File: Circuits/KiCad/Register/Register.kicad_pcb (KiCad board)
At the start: 2 copper layers, 55.2 x 52.1 mm, 7 parts, among them J1 Conn_01x13_Male, J2 Conn_01x02_Male, J3 Conn_01x02_Male, U1 74LS377f, U2 74LS245

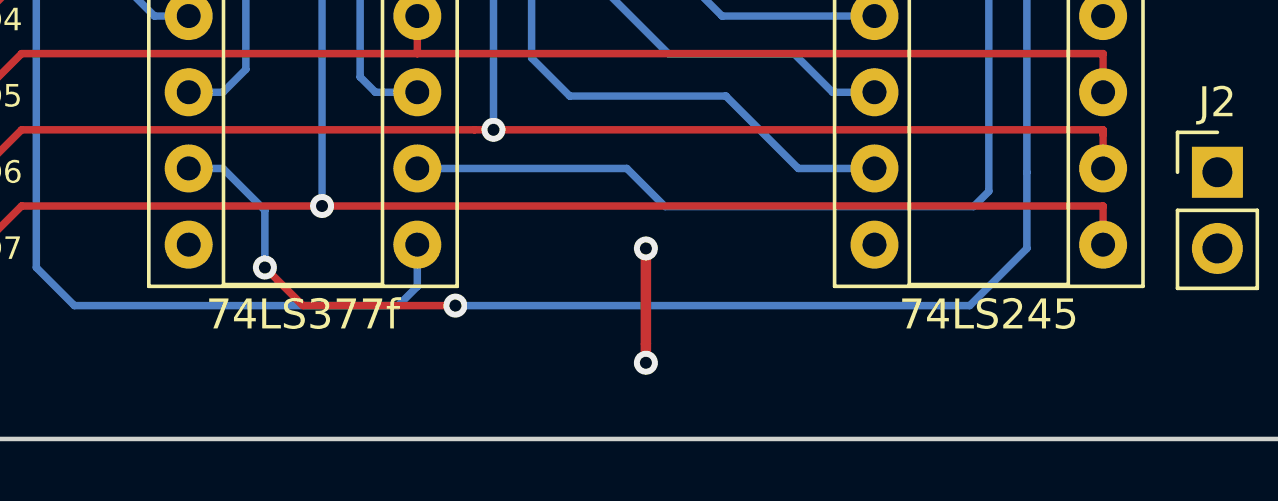
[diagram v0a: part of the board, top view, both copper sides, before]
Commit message: Added Stack Pointer schematics & PCB. Rerouted Clock based autorouter output
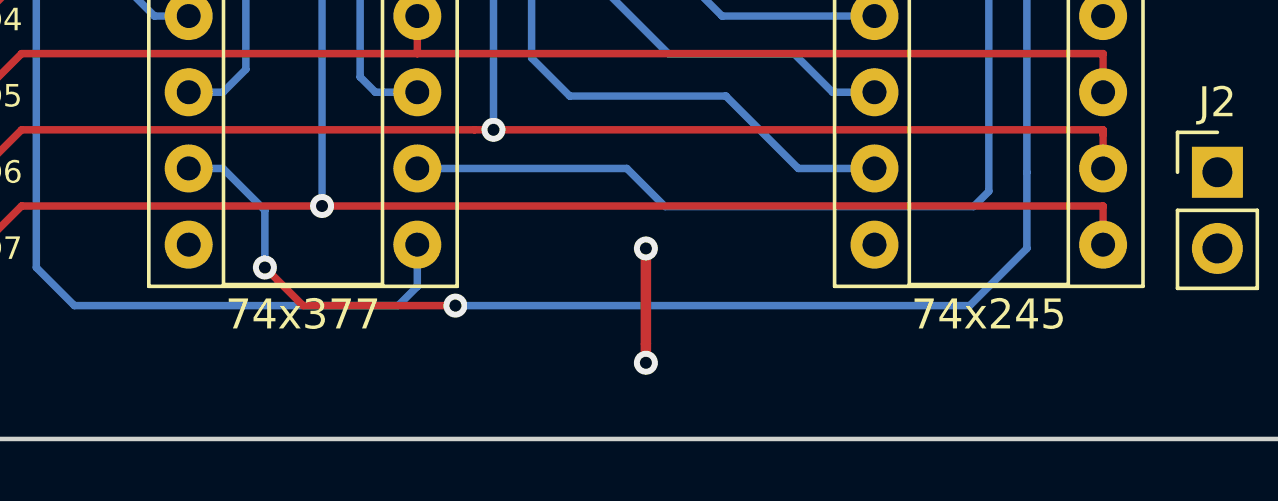
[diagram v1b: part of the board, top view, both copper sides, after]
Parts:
- U1: value 74LS377f -> 74x377
- U2: value 74LS245 -> 74x245
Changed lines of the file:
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@@
       (effects (font (size 1 1) (thickness 0.15)))
     )
-    (fp_text value 74LS245 (at 3.81 25.19) (layer F.SilkS)
+    (fp_text value 74x245 (at 3.81 25.19) (layer F.SilkS)
       (effects (font (size 1 1) (thickness 0.15)))
     )
@@
       (effects (font (size 1 1) (thickness 0.15)))
     )
-    (fp_text value 74LS377f (at 3.81 25.19) (layer F.SilkS)
+    (fp_text value 74x377 (at 3.81 25.19) (layer F.SilkS)
       (effects (font (size 1 1) (thickness 0.15)))
     )

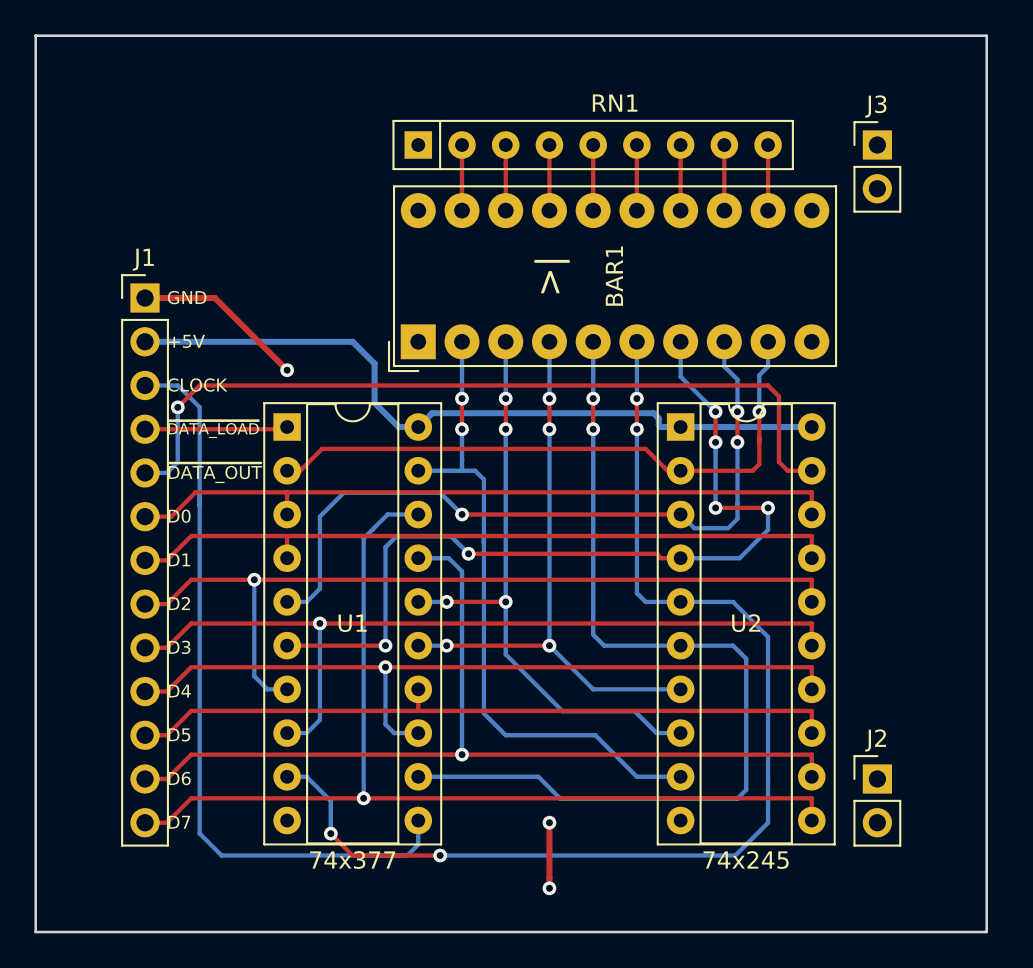
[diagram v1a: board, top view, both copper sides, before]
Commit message: Made sure spacing between headers is always 2.54mm pitch
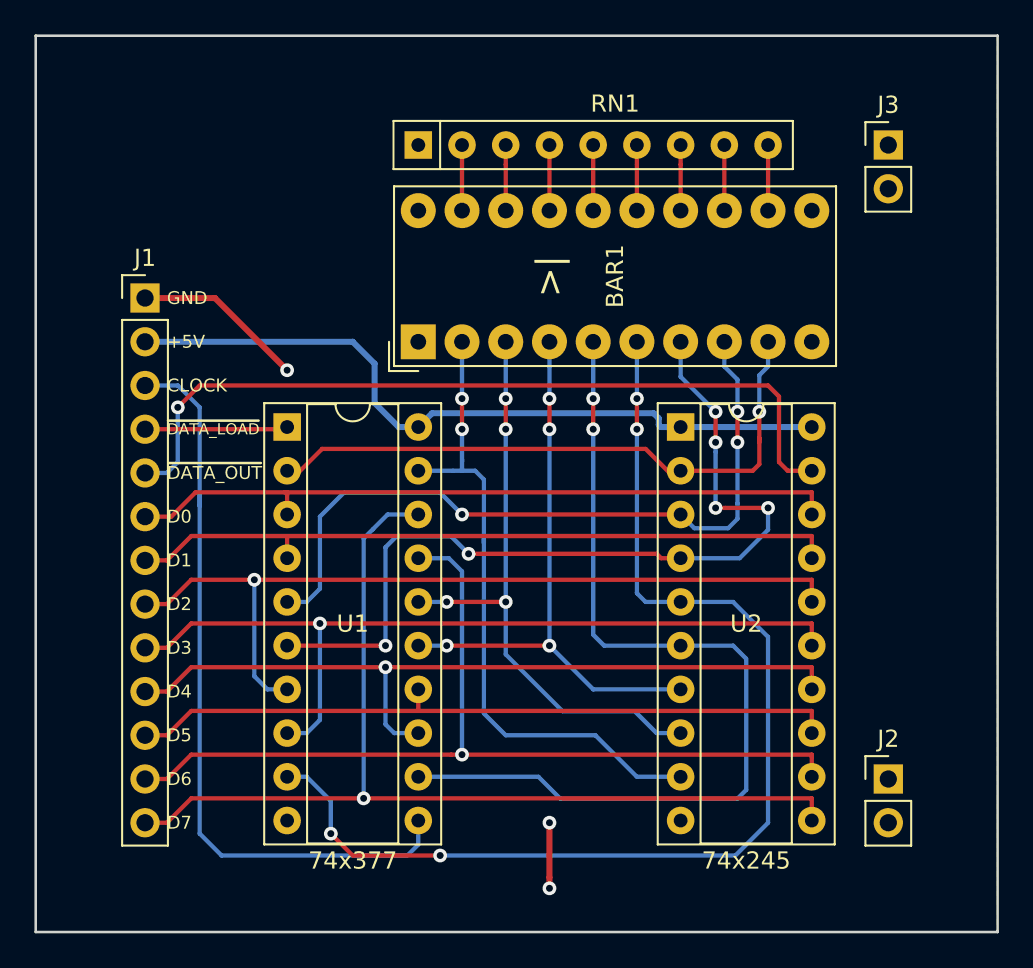
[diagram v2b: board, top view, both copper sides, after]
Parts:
- moved J2 0.63 mm to (76.8, 61.0)
- moved J3 0.63 mm to (76.8, 24.1)
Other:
- board size 55.2 x 52.1 mm -> 55.9 x 52.1 mm
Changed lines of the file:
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@@
   )
   (module Connector_PinHeader_2.54mm:PinHeader_1x02_P2.54mm_Vertical (layer F.Cu)
-    (at 76.2 24.13)
+    (at 76.835 24.13)
     (descr "Through hole straight pin header, 1x02, 2.54mm pitch, single row")
     (tags "Through hole pin header THT 1x02 2.54mm single row")
@@
   )
   (module Connector_PinHeader_2.54mm:PinHeader_1x02_P2.54mm_Vertical (layer F.Cu)
-    (at 76.2 60.96)
+    (at 76.835 60.96)
     (descr "Through hole straight pin header, 1x02, 2.54mm pitch, single row")
     (tags "Through hole pin header THT 1x02 2.54mm single row")
@@
   )
   (gr_line (start 27.305 69.85) (end 27.305 17.78) (layer Edge.Cuts) (width 0.15))
-  (gr_line (start 82.55 69.85) (end 27.305 69.85) (layer Edge.Cuts) (width 0.15))
-  (gr_line (start 82.55 17.78) (end 82.55 69.85) (layer Edge.Cuts) (width 0.15))
-  (gr_line (start 27.305 17.78) (end 82.55 17.78) (layer Edge.Cuts) (width 0.15))
+  (gr_line (start 83.185 69.85) (end 27.305 69.85) (layer Edge.Cuts) (width 0.15))
+  (gr_line (start 83.185 17.78) (end 83.185 69.85) (layer Edge.Cuts) (width 0.15))
+  (gr_line (start 27.305 17.78) (end 83.185 17.78) (layer Edge.Cuts) (width 0.15))
   (gr_text >| (at 57.15 31.75 90) (layer F.SilkS)
     (effects (font (size 1.5 1.5) (thickness 0.3)))
   )
-  (gr_poly (pts (xy 77.47 64.77) (xy 82.47 64.77) (xy 82.47 69.77) (xy 77.47 69.77)) (layer Margin) (width 0.15))
-  (gr_poly (pts (xy 77.47 17.86) (xy 82.47 17.86) (xy 82.47 22.86) (xy 77.47 22.86)) (layer Margin) (width 0.15))
+  (gr_poly (pts (xy 78.105 64.77) (xy 83.105 64.77) (xy 83.105 69.77) (xy 78.105 69.77)) (layer Margin) (width 0.15))
+  (gr_poly (pts (xy 78.105 17.86) (xy 83.105 17.86) (xy 83.105 22.86) (xy 78.105 22.86)) (layer Margin) (width 0.15))
   (gr_poly (pts (xy 27.385 17.86) (xy 32.385 17.86) (xy 32.385 22.86) (xy 27.385 22.86)) (layer Margin) (width 0.15))
   (gr_poly (pts (xy 27.305 64.85) (xy 32.305 64.85) (xy 32.305 69.85) (xy 27.305 69.85)) (layer Margin) (width 0.15))
@@
     (polygon
       (pts
-        (xy 27.305 17.78) (xy 82.55 17.78) (xy 82.55 69.85) (xy 27.305 69.85)
+        (xy 27.305 17.78) (xy 83.185 17.78) (xy 83.185 69.85) (xy 27.305 69.85)
       )
     )

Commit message: Rerouted Register PCB and fixed pin header pitch
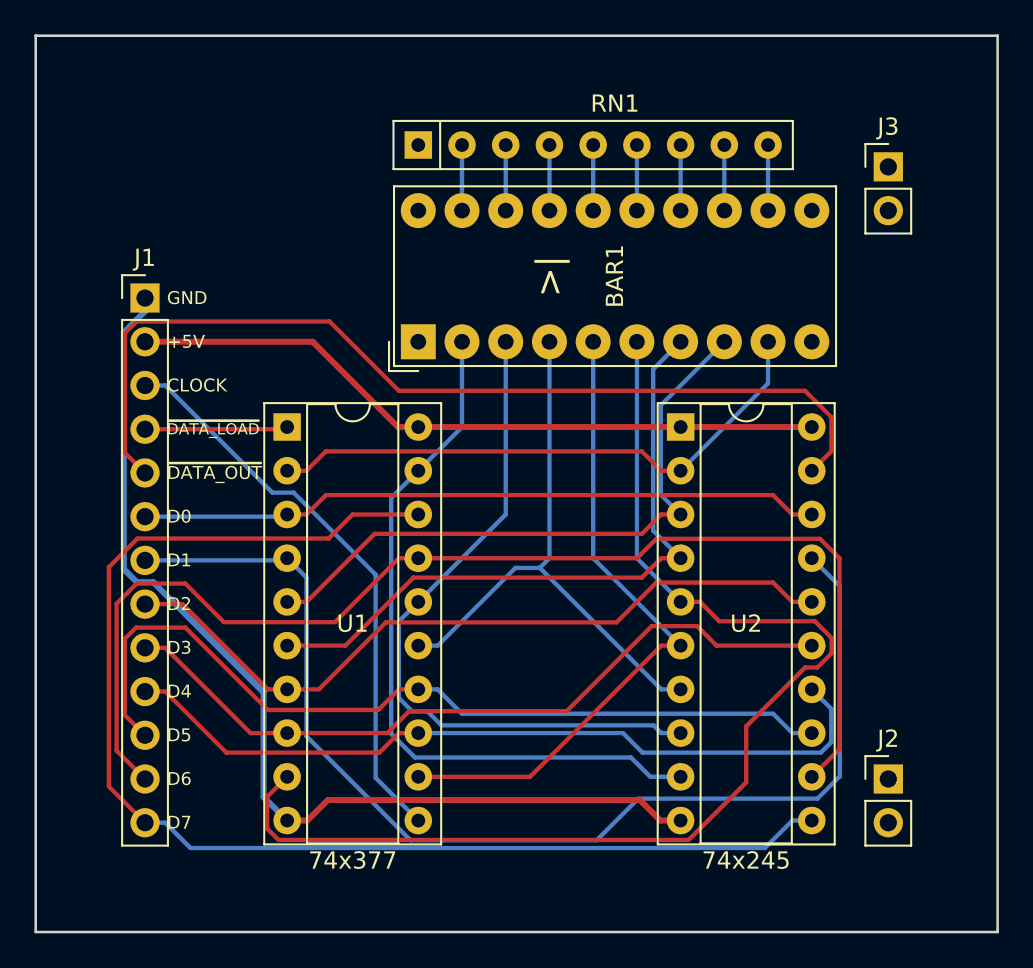
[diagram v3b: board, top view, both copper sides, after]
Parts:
- moved J3 1.27 mm to (76.8, 25.4)
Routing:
- net GND: track 13.8 -> 59.2 mm, vias 3 -> 0
- net Net-(J1-Pad7): track 41.9 -> 67.5 mm
- net Net-(J1-Pad12): track 54.1 -> 70.1 mm, vias 1 -> 0
- net Net-(BAR1-Pad5): track 53.9 -> 38.2 mm, vias 2 -> 0
- net Net-(J1-Pad13): track 59.6 -> 75.0 mm, vias 1 -> 0
- net Net-(BAR1-Pad7): track 49.9 -> 38.9 mm, vias 6 -> 0
- net CLOCK: track 44.0 -> 33.3 mm
- net ~DATA_OUT: track 47.0 -> 55.8 mm, vias 1 -> 0
- net Net-(J1-Pad11): track 41.9 -> 49.8 mm
- net Net-(BAR1-Pad8): track 42.9 -> 37.0 mm, vias 3 -> 0
- net Net-(BAR1-Pad3): track 35.3 -> 40.5 mm, vias 4 -> 0
- net Net-(J1-Pad8): track 48.3 -> 43.8 mm, vias 1 -> 0
- net Net-(J1-Pad9): track 48.3 -> 43.8 mm, vias 1 -> 0
- net Net-(BAR1-Pad2): track 38.3 -> 42.3 mm, vias 2 -> 0
- net Net-(BAR1-Pad6): track 65.8 -> 69.6 mm, vias 4 -> 0
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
